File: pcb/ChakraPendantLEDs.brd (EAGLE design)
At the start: 25.4 x 25.4 mm, 11 parts

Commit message: Flip the terminals, because they will be mirrored.
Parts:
- moved CLK 13.2 mm to (6.10, 21.8)
- moved VCC 13.2 mm to (19.3, 21.8)
- moved DAT 8.64 mm to (8.38, 23.1)
- moved GND 8.64 mm to (17.0, 23.1)
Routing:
- net GND: track 0.00 -> 5.62 mm, vias 0 -> 1
- net CLK: track 14.0 -> 11.1 mm
- net DAT: track 12.5 -> 9.67 mm
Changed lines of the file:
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@@
 <text x="12.7" y="6.096" size="1.4224" layer="26" rot="MR0" align="center">Chakra
 Pendant</text>
-<text x="6.858" y="20.066" size="0.8128" layer="25">V+</text>
-<text x="8.89" y="21.844" size="0.8128" layer="25" rot="R180">G</text>
-<text x="17.272" y="21.844" size="0.8128" layer="25" rot="R180">D</text>
-<text x="18.542" y="20.828" size="0.8128" layer="25" rot="R180">C</text>
+<text x="19.304" y="20.574" size="0.8128" layer="25" rot="R180">V+</text>
+<text x="17.526" y="21.844" size="0.8128" layer="25" rot="R180">G</text>
+<text x="9.144" y="21.844" size="0.8128" layer="25" rot="R180">D</text>
+<text x="7.62" y="20.828" size="0.8128" layer="25" rot="R180">C</text>
 </plain>
 <attributes>
@@
 <attribute name="VALUE" x="8.533215625" y="12.854946875" size="1.27" layer="27" font="vector" rot="R60"/>
 </element>
-<element name="DAT" library="SparkFun-Connectors" package="1X01NS" value="M01SMDNS" x="17.018" y="23.114"/>
-<element name="CLK" library="SparkFun-Connectors" package="1X01NS" value="M01SMDNS" x="19.304" y="21.844"/>
-<element name="GND" library="SparkFun-Connectors" package="1X01NS" value="M01SMDNS" x="8.382" y="23.114"/>
-<element name="VCC" library="SparkFun-Connectors" package="1X01NS" value="M01SMDNS" x="6.096" y="21.844"/>
+<element name="DAT" library="SparkFun-Connectors" package="1X01NS" value="M01SMDNS" x="8.382" y="23.114"/>
+<element name="CLK" library="SparkFun-Connectors" package="1X01NS" value="M01SMDNS" x="6.096" y="21.844"/>
+<element name="GND" library="SparkFun-Connectors" package="1X01NS" value="M01SMDNS" x="17.018" y="23.114"/>
+<element name="VCC" library="SparkFun-Connectors" package="1X01NS" value="M01SMDNS" x="19.304" y="21.844"/>
 </elements>
 <signals>
@@
 <contactref element="U$7" pad="GND"/>
 <contactref element="GND" pad="1"/>
+<wire x1="17.018" y1="23.114" x2="17.04685" y2="23.114" width="0.4064" layer="16"/>
+<wire x1="17.04685" y1="23.114" x2="17.04685" y2="17.51905" width="0.4064" layer="16"/>
+<via x="17.04685" y="17.51905" extent="1-16" drill="0.5"/>
 </signal>
 <signal name="DAT">
 <contactref element="U$1" pad="DAT-IN"/>
 <via x="10.7" y="14.4" extent="1-16" drill="0.5"/>
-<wire x1="17.018" y1="18.796" x2="12.622" y2="14.4" width="0.4064" layer="16"/>
-<wire x1="12.622" y1="14.4" x2="10.7" y2="14.4" width="0.4064" layer="16"/>
 <contactref element="DAT" pad="1"/>
-<wire x1="17.018" y1="18.796" x2="17.018" y2="23.114" width="0.4064" layer="16"/>
+<wire x1="8.382" y1="23.114" x2="10.7" y2="20.796" width="0.4064" layer="16"/>
+<wire x1="10.7" y1="20.796" x2="10.7" y2="14.4" width="0.4064" layer="16"/>
 </signal>
 <signal name="CLK">
 <contactref element="U$1" pad="CLK-IN"/>
 <via x="10.7" y="12.7" extent="1-16" drill="0.5"/>
-<wire x1="19.304" y1="19.05" x2="12.954" y2="12.7" width="0.4064" layer="16"/>
-<wire x1="12.954" y1="12.7" x2="10.7" y2="12.7" width="0.4064" layer="16"/>
 <contactref element="CLK" pad="1"/>
-<wire x1="19.304" y1="19.05" x2="19.304" y2="21.844" width="0.4064" layer="16"/>
+<wire x1="6.096" y1="21.844" x2="9.652" y2="18.288" width="0.4064" layer="16"/>
+<wire x1="9.652" y1="18.288" x2="9.652" y2="13.748" width="0.4064" layer="16"/>
+<wire x1="9.652" y1="13.748" x2="10.7" y2="12.7" width="0.4064" layer="16"/>
 </signal>
 <signal name="VCC">

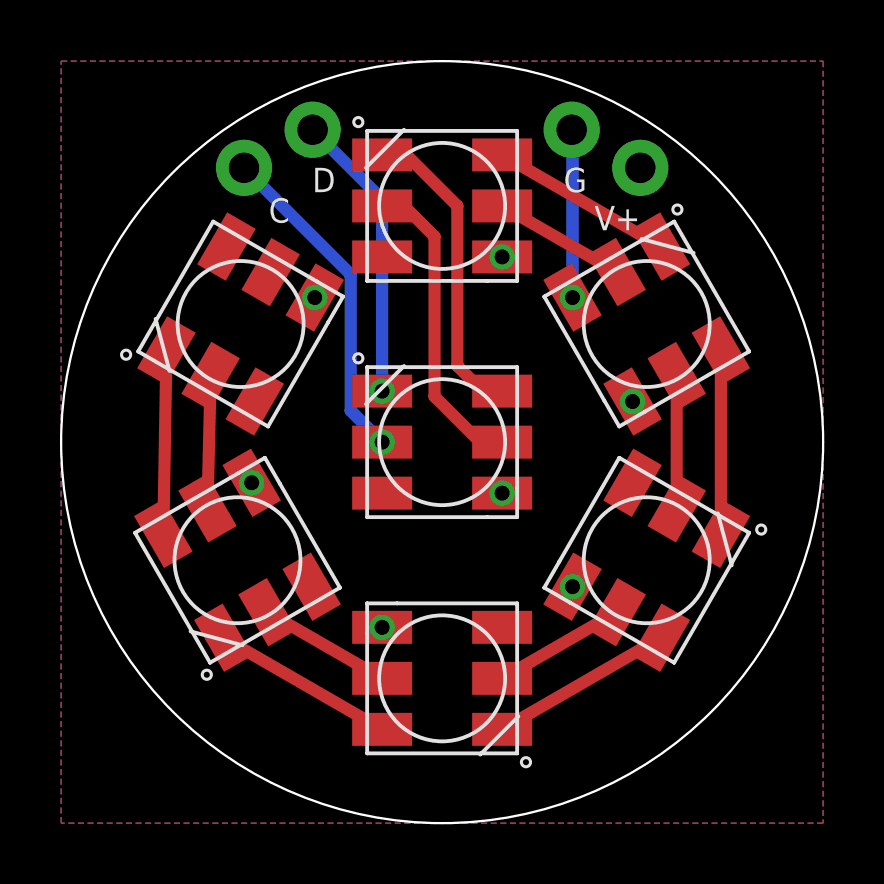
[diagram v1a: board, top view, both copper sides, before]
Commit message: GREATLY cleaned up main board schematic. Piped charge STAT to chip
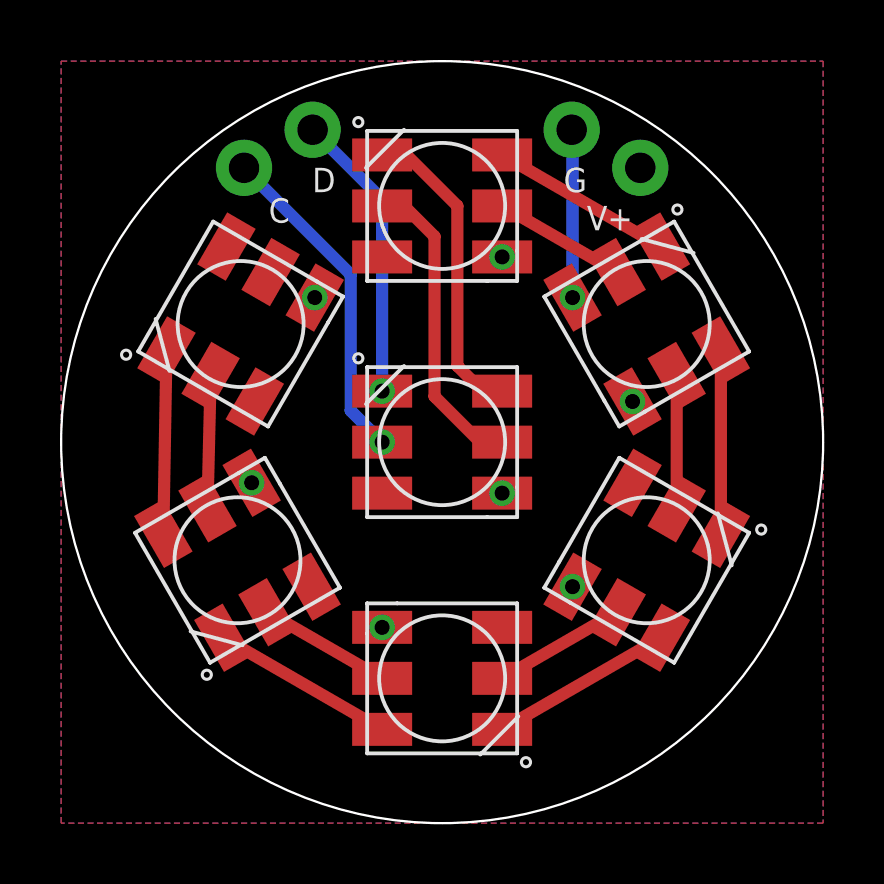
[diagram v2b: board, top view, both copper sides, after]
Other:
- board text added: "LED Board v3 2015.01.10"
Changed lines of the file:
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@@
 <grid distance="0.01" unitdist="inch" unit="inch" style="dots" multiple="1" display="no" altdistance="0.01" altunitdist="inch" altunit="inch"/>
 <layers>
-<layer number="1" name="Top" color="4" fill="1" visible="yes" active="yes"/>
+<layer number="1" name="Top" color="4" fill="1" visible="no" active="yes"/>
 <layer number="16" name="Bottom" color="1" fill="1" visible="yes" active="yes"/>
 <layer number="17" name="Pads" color="2" fill="1" visible="yes" active="yes"/>
 <layer number="18" name="Vias" color="2" fill="1" visible="yes" active="yes"/>
-<layer number="19" name="Unrouted" color="6" fill="1" visible="yes" active="yes"/>
+<layer number="19" name="Unrouted" color="6" fill="1" visible="no" active="yes"/>
 <layer number="20" name="Dimension" color="15" fill="1" visible="yes" active="yes"/>
 <layer number="21" name="tPlace" color="7" fill="1" visible="no" active="yes"/>
-<layer number="22" name="bPlace" color="7" fill="1" visible="no" active="yes"/>
+<layer number="22" name="bPlace" color="7" fill="1" visible="yes" active="yes"/>
 <layer number="23" name="tOrigins" color="15" fill="1" visible="no" active="yes"/>
-<layer number="24" name="bOrigins" color="15" fill="1" visible="no" active="yes"/>
+<layer number="24" name="bOrigins" color="15" fill="1" visible="yes" active="yes"/>
 <layer number="25" name="tNames" color="7" fill="1" visible="no" active="yes"/>
-<layer number="26" name="bNames" color="7" fill="1" visible="no" active="yes"/>
+<layer number="26" name="bNames" color="7" fill="1" visible="yes" active="yes"/>
 <layer number="27" name="tValues" color="7" fill="1" visible="no" active="yes"/>
 <layer number="28" name="bValues" color="7" fill="1" visible="no" active="yes"/>
@@
 <layer number="43" name="vRestrict" color="2" fill="10" visible="no" active="yes"/>
 <layer number="44" name="Drills" color="7" fill="1" visible="no" active="yes"/>
-<layer number="45" name="Holes" color="7" fill="1" visible="no" active="yes"/>
-<layer number="46" name="Milling" color="3" fill="1" visible="no" active="yes"/>
+<layer number="45" name="Holes" color="7" fill="1" visible="yes" active="yes"/>
+<layer number="46" name="Milling" color="3" fill="1" visible="yes" active="yes"/>
 <layer number="47" name="Measures" color="7" fill="1" visible="no" active="yes"/>
 <layer number="48" name="Document" color="7" fill="1" visible="no" active="yes"/>
@@
 <text x="12.7" y="6.096" size="1.4224" layer="26" rot="MR0" align="center">Chakra
 Pendant</text>
-<text x="19.304" y="20.574" size="0.8128" layer="25" rot="R180">V+</text>
+<text x="19.05" y="20.574" size="0.8128" layer="25" rot="R180">V+</text>
 <text x="17.526" y="21.844" size="0.8128" layer="25" rot="R180">G</text>
 <text x="9.144" y="21.844" size="0.8128" layer="25" rot="R180">D</text>
 <text x="7.62" y="20.828" size="0.8128" layer="25" rot="R180">C</text>
+<text x="12.954" y="18.796" size="0.8128" layer="22" rot="MR0" align="center">LED Board
+v3
+2015.01.10</text>
 </plain>
 <attributes>
